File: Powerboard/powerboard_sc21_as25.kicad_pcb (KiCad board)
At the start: 4 copper layers, 86.1 x 55.6 mm, 172 parts, among them IC1 BQ24618RGET-iclr, IC2 CP2102, J1 Thermistor Connection 103AT N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, J10 Conn_01x04_Male, J2 Conn_01x02_Male, J3 Conn_01x02_Male, J4 Conn_01x08_Male, J5 Conn_01x04_Male, J6 Conn_01x02_Male, J7 IsolationSwitch, J8 USB_C_Receptacle_USB2.0, J9 Conn_Coaxial, Q1 RSJ250P10TL, Q10 MCH6351, Q2 RSJ250P10TL, Q3 RSJ250P10TL, Q4 RS1G120MN, Q5 RS1G120MN, Q6 MMDT2222A, Q7 RSJ250P10TL, Q8 RSJ250P10TL, Q9 MCH6351, U1 LTC4412xS6, U11 LTC4411, U2 SN65HVD230, U3 ESP32-PICO-D4, U4 RT9025-25GSP, U6 LM2679T-3.3-iclr, U7 LM2679T-3.3-iclr, U8 LTC4412xS6, U9 LTC4412xS6

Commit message: layout progress
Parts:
- C31, C32, R30, R31, U4: moved to B.Cu
- D7, R36, R37, TP23, TP24: moved to F.Cu
- RAC1: value 10mΩ -> FCSL110R010FER; footprint Resistor_SMD:R_0603_1608Metric -> iclr:RESC50110X50N
- moved U8 76.2 mm to (129.8, 72.7)
- moved C48 75.4 mm to (127.0, 72.9), turned to -90 degrees
- moved Q10 72.7 mm to (127.5, 75.8), turned to 180 degrees
- moved C44 69.2 mm to (131.3, 64.4), turned to -90 degrees
- moved D5 66.5 mm to (128.3, 66.8)
- moved C9 63.9 mm to (72.1, 69.4), turned to 0 degrees
- moved C8 62.5 mm to (72.2, 67.4), turned to 0 degrees
- moved C37 61.4 mm to (116.0, 61.9), turned to 180 degrees
- moved U7 60.9 mm to (118.2, 52.5), turned to 90 degrees
- moved C49 60.0 mm to (126.1, 49.9)
- moved U9 59.9 mm to (126.6, 52.3)
- moved Q9 59.8 mm to (130.1, 52.4), turned to -90 degrees
- moved C42 59.3 mm to (104.9, 45.8), turned to 0 degrees
- moved C45 57.9 mm to (122.8, 42.7), turned to -90 degrees
- moved TP19 57.1 mm to (10.1, 43.3)
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- renumbered C15 to Crr
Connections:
- C3 pad 1: Net-(C3-Pad1) -> Net-(C33-Pad2)
- C33 pad 2: Net-(C3-Pad1) -> Net-(C33-Pad2)
- IC1 pad 2: Net-(C3-Pad1) -> Net-(C33-Pad2)
- J4 pad 1: /CANH -> GND
- J4 pad 2: /CANH -> GND
- J4 pad 4: Net-(J4-Pad4) -> /CANL
- J4 pad 5: +3V3 -> Net-(J4-Pad5)
- J4 pad 6: +3V3 -> Net-(J4-Pad5)
- J4 pad 7: /CANL -> +3V3
- J4 pad 8: /CANL -> /CANH
- Q2 pad 3: Net-(C3-Pad1) -> Net-(C33-Pad2)
- Q7 pad 3: Net-(J4-Pad4) -> Net-(Q7-Pad3)
- RAC1 pad 1: +24V -> Net-(C33-Pad2)
- RAC1 pad 2: Net-(C3-Pad1) -> +24V
- U1 pad 6: Net-(J4-Pad4) -> Net-(Q7-Pad3)
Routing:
- net +24V: track 0.00 -> 150.5 mm, vias 0 -> 2
- net /SDA: track 0.00 -> 74.0 mm, vias 0 -> 2
- net +3V3: track 10.7 -> 84.3 mm
- net /Battery Charger/Q3-S: track 0.00 -> 64.6 mm, vias 0 -> 2
- net /SCL: track 0.00 -> 64.2 mm, vias 0 -> 2
- net /BATTSTAT2: track 0.00 -> 60.2 mm, vias 0 -> 1
- net /CHARGE: track 0.13 -> 58.4 mm
- net /BATTSTAT1: track 0.00 -> 55.7 mm, vias 0 -> 1
- net /3.3STAT2: track 0.00 -> 54.1 mm, vias 0 -> 3
- net Net-(IC1-Pad23): track 0.00 -> 54.0 mm, vias 0 -> 2
- net /Battery Charger/Q1-D: track 0.00 -> 52.7 mm
- net Net-(C39-Pad1): track 0.00 -> 49.7 mm
- net /BOOT: track 0.00 -> 48.9 mm, vias 0 -> 4
- net /3.3STAT1: track 0.00 -> 44.0 mm, vias 0 -> 3
- net Net-(C18-Pad2): track 0.00 -> 42.8 mm, vias 0 -> 2
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- added copper zone on F.Cu, net Net-(C31-Pad1)
- added copper zone on F.Cu, net Net-(J5-Pad1)
- added copper zone on F.Cu, net Net-(Q7-Pad3)

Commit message: update
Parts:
- removed Crr: 0.1µF, Capacitor_SMD:C_0603_1608Metric
- removed TP1, TP10, TP11, TP12, TP13, TP16, TP17, TP18, TP19, TP2, TP20, TP21, TP22, TP26, TP27, TP3, TP4, TP5, TP6, TP7, TP8, TP9: TestPoint, TestPoint:TestPoint_Pad_D1.0mm
- added C15: 0.1µF, Capacitor_SMD:C_0603_1608Metric, F.Cu at (72.6, 71.9)
- moved PackLED1 10.4 mm to (72.8, 81.7), turned to 0 degrees
- moved C48 9.31 mm to (127.6, 63.6), turned to 0 degrees
- moved R28 8.97 mm to (69.8, 81.7), turned to 180 degrees
- moved U8 6.83 mm to (128.2, 66.0)
- moved Q10 6.67 mm to (127.7, 69.2)
- moved D5 6.23 mm to (130.0, 72.8), turned to -90 degrees
- moved C17 2.17 mm to (96.3, 46.1)
- moved R6 2.17 mm to (94.8, 46.1)
- moved C1 1.90 mm to (80.2, 31.7), turned to 90 degrees
- moved C49 1.87 mm to (127.2, 48.4)
- moved C2 1.63 mm to (96.3, 43.1)
- moved R4 1.63 mm to (94.8, 43.1)
- moved C53 1.58 mm to (63.3, 68.1)
- moved C21 0.93 mm to (93.3, 66.3)
- moved C24 0.79 mm to (87.3, 47.1)
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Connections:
- J8 pad A1: Net-(J8-PadA1) -> GND
- J8 pad A12: Net-(J8-PadA1) -> GND
- J8 pad B1: Net-(J8-PadA1) -> GND
- J8 pad B12: Net-(J8-PadA1) -> GND
- J8 pad S1: unconnected-(J8-PadS1) -> GND
- PowerLED1 pad 2: Net-(PowerLED1-Pad2) -> Net-(J5-Pad1)
- Q1 pad 3: Net-(PowerLED1-Pad2) -> Net-(J5-Pad1)
- R20 pad 2: Net-(PowerLED1-Pad2) -> Net-(J5-Pad1)
- U3 pad 16: unconnected-(U3-Pad16) -> GND
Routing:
- net /EN: track 0.00 -> 70.3 mm, vias 0 -> 6
- net GND: track 1.11 -> 71.1 mm, vias 0 -> 19
- net Net-(IC1-Pad3): track 0.00 -> 69.3 mm, vias 0 -> 2
- net /Battery Charger/VFB: track 2.96 -> 71.8 mm, vias 0 -> 2
- net Net-(C17-Pad2): track 0.00 -> 60.2 mm, vias 0 -> 2
- net VBUS: track 7.41 -> 49.2 mm
- net /Battery Charger/VCC: track 0.00 -> 34.9 mm, vias 0 -> 2
- net /Battery Charger/Q3-S: track 64.6 -> 99.1 mm, vias 2 -> 8
- net Net-(Q7-Pad1): track 0.00 -> 30.4 mm, vias 0 -> 2
- net +3V3: track 84.3 -> 105.5 mm, vias 0 -> 19
- net Net-(IC1-Pad11): track 0.00 -> 18.9 mm
- net /Battery Charger/ACSET: track 0.00 -> 18.6 mm
- net Net-(C39-Pad1): track 49.7 -> 67.3 mm
- net /Battery Charger/ICSET2: track 0.00 -> 16.6 mm
- net Net-(Q7-Pad3): track 0.00 -> 15.9 mm
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- added copper zone on F.Cu, net +24V
- added copper zone on In2.Cu, net +3V3
- added copper zone on F.Cu, net /Battery Charger/Q3-S
- added copper zone on B.Cu, net GND
- added copper zone on F.Cu, net GND
- added copper zone on In1.Cu, net GND
- added copper zone on F.Cu, net Net-(C3-Pad1)

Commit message: update
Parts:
- C1, C10, C11, C3, C31, C33: value 0.1μF -> 0.1uF
- C14, C15, C48, C49, C6: value 0.1µF -> 0.1uF
- C17, C18, C2, C4: value 1μF -> 1uF
- C32: value 22μF -> 22uF; footprint Capacitor_SMD:C_1210_3225Metric -> Capacitor_SMD:C_1206_3216Metric
- C43: value 0.47μF -> 0.47uF
- C50: value 1.0muF -> 1.0uF
- C51, C53: value 0.1muF -> 0.1uF
- C52: value 4.7muF -> 4.7uF
- C54, C57: footprint Capacitor_SMD:C_0805_2012Metric -> Capacitor_SMD:C_0603_1608Metric
- L1: value 6.8µH -> 6.8uH
- R1, R11, R4: value 10kΩ -> 10k
- R10: value 430kΩ -> 430k
- R14, R15, R3, R5, R7: value 100kΩ -> 100k
- R16: value 100Ω -> 100
- R17: value 10Ω -> 10
- R18, R32: value 1kΩ -> 1k
- R19, R21, R37, R6, R8: value 470Ω -> 470
- R2: value 110kΩ -> 110k
- R20: value 2Ω -> 2
- R28, R29: value 3.5k -> 3k
- R9: value 9.31kΩ -> 9.31k
- RAdp1: value 150kΩ -> 150k
- RFast1: value 32kΩ -> 32k
- RPre1: value 13kΩ -> 13k
- RSR1: value 10mΩ -> 10m
- U4: value RT9025-25GSP -> SC4216H
- moved H1 2.53 mm to (52.1, 43.6)
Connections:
- net Net-(D8-Pad3) renamed /USB To UART/D-
- net Net-(D8-Pad4) renamed /USB To UART/D+
- IC2 pad 29: unconnected-(IC2-Pad29) -> GND
- J4 pad 5: Net-(J4-Pad5) -> Net-(U1-Pad6)
- J4 pad 6: Net-(J4-Pad5) -> Net-(U1-Pad6)
- Q7 pad 3: Net-(Q7-Pad3) -> Net-(U1-Pad6)
- R22 pad 2: Net-(C21-Pad2) -> Net-(R22-Pad2)
- U1 pad 3: /LPC_24V -> unconnected-(U1-Pad3)
- U1 pad 6: Net-(Q7-Pad3) -> Net-(U1-Pad6)
- U2 pad 1: Net-(C21-Pad2) -> Net-(R22-Pad2)
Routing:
- net /LPC_24V: track 43.1 -> 0.00 mm, vias 3 -> 0
- net unconnected-(U1-Pad3): track 0.00 -> 42.7 mm, vias 0 -> 3
- net Net-(Q7-Pad3): track 15.9 -> 0.00 mm
- net Net-(U1-Pad6): track 0.00 -> 15.7 mm
- net /Battery Charger/Q3-S: track 99.1 -> 105.6 mm
- net GND: track 71.1 -> 65.5 mm, vias 19 -> 17
- net +3V3: track 105.5 -> 110.6 mm, vias 19 -> 20
- net Net-(R22-Pad2): track 0.00 -> 3.50 mm
- net Net-(C21-Pad2): track 3.50 -> 0.00 mm
- net /EN: track 70.3 -> 72.5 mm
- net /BOOT: track 61.4 -> 63.6 mm
- net +24V: track 153.7 -> 155.1 mm
- net Net-(J5-Pad1): track 8.94 -> 10.2 mm
- net /PG: track 45.9 -> 44.9 mm
- net /Battery Charger/SRP: track 22.3 -> 21.3 mm
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- added copper zone on F.Cu, net Net-(U1-Pad6)
- removed copper zone on F.Cu, net Net-(Q7-Pad3)

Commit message: update 2
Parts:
- removed C21: 160pF, Capacitor_SMD:C_0603_1608Metric
- moved C58 1.60 mm to (61.8, 40.6), turned to 0 degrees
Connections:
- U1 pad 3: unconnected-(U1-Pad3) -> /LPC_24V
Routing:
- net /LPC_24V: track 0.00 -> 43.0 mm, vias 0 -> 3
- net unconnected-(U1-Pad3): track 42.7 -> 0.00 mm, vias 3 -> 0
- net Net-(IC1-Pad3): track 68.6 -> 63.3 mm
- net /Battery Charger/Q3-S: track 105.6 -> 102.9 mm, vias 8 -> 7
- net GND: track 65.5 -> 63.8 mm, vias 17 -> 18
- net Net-(R22-Pad2): track 3.50 -> 2.18 mm
- net /SCL: track 62.3 -> 63.2 mm
- net /CHARGE: track 59.7 -> 60.5 mm
- net /BATTSTAT1: track 57.9 -> 57.3 mm
- net /CANH: track 25.2 -> 24.6 mm
- net /CANL: track 39.5 -> 38.9 mm
- net Net-(IC1-Pad23): track 53.4 -> 52.9 mm

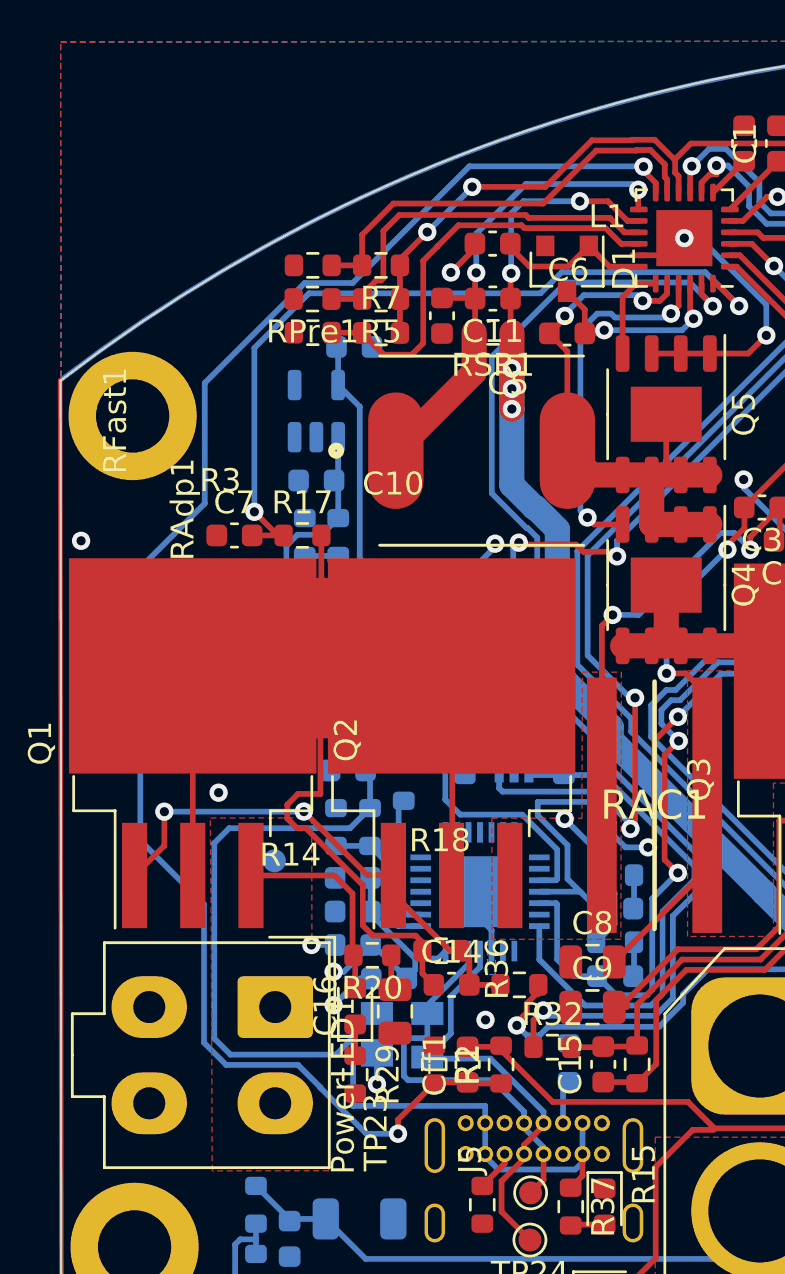
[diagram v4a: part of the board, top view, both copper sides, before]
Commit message: changed RSR traces to same layer
going to check charger layout recommendations again
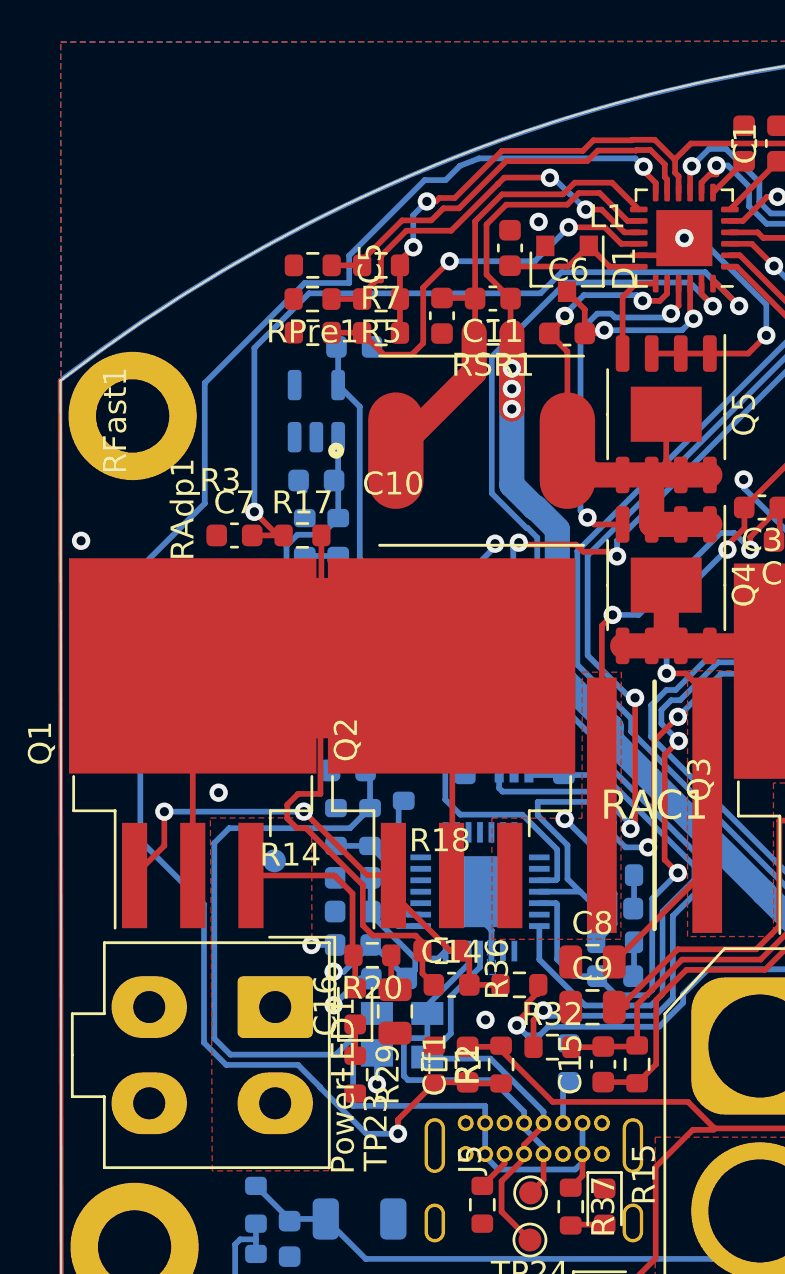
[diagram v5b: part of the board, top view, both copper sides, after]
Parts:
- moved C5 0.78 mm to (68.5, 36.2), turned to 90 degrees
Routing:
- net GND: track 63.8 -> 62.1 mm
- net /Battery Charger/Q3-S: track 102.9 -> 104.5 mm, vias 7 -> 5
- net /Battery Charger/VFB: track 71.5 -> 72.4 mm
- net /Battery Charger/CE: track 37.5 -> 38.2 mm
- net /Battery Charger/ICSET2: track 16.6 -> 17.4 mm, vias 0 -> 2
- net /Battery Charger/ACSET: track 18.6 -> 17.8 mm, vias 0 -> 2
- net Net-(IC1-Pad11): track 18.9 -> 18.3 mm
- net /Battery Charger/SRP: track 21.3 -> 21.2 mm, vias 2 -> 0

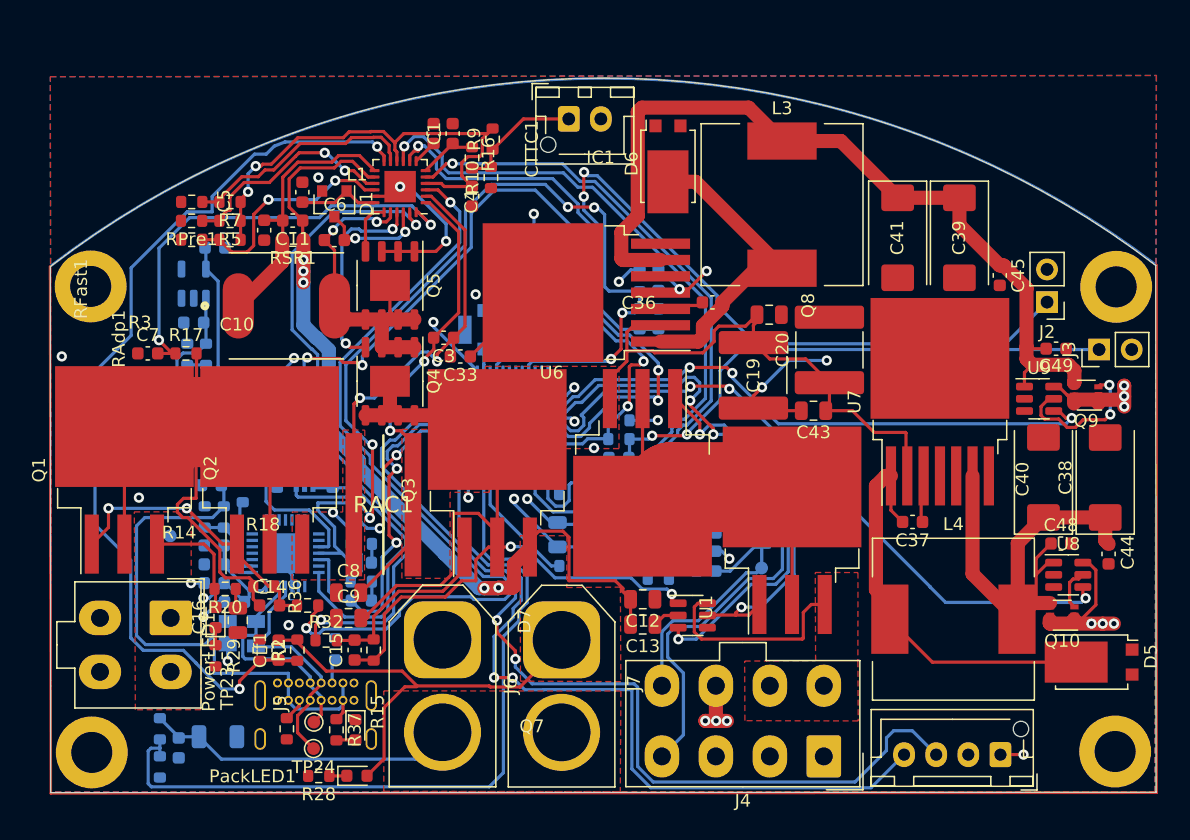
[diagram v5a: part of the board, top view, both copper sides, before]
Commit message: Andrei's review, no via fencing on ufl conn
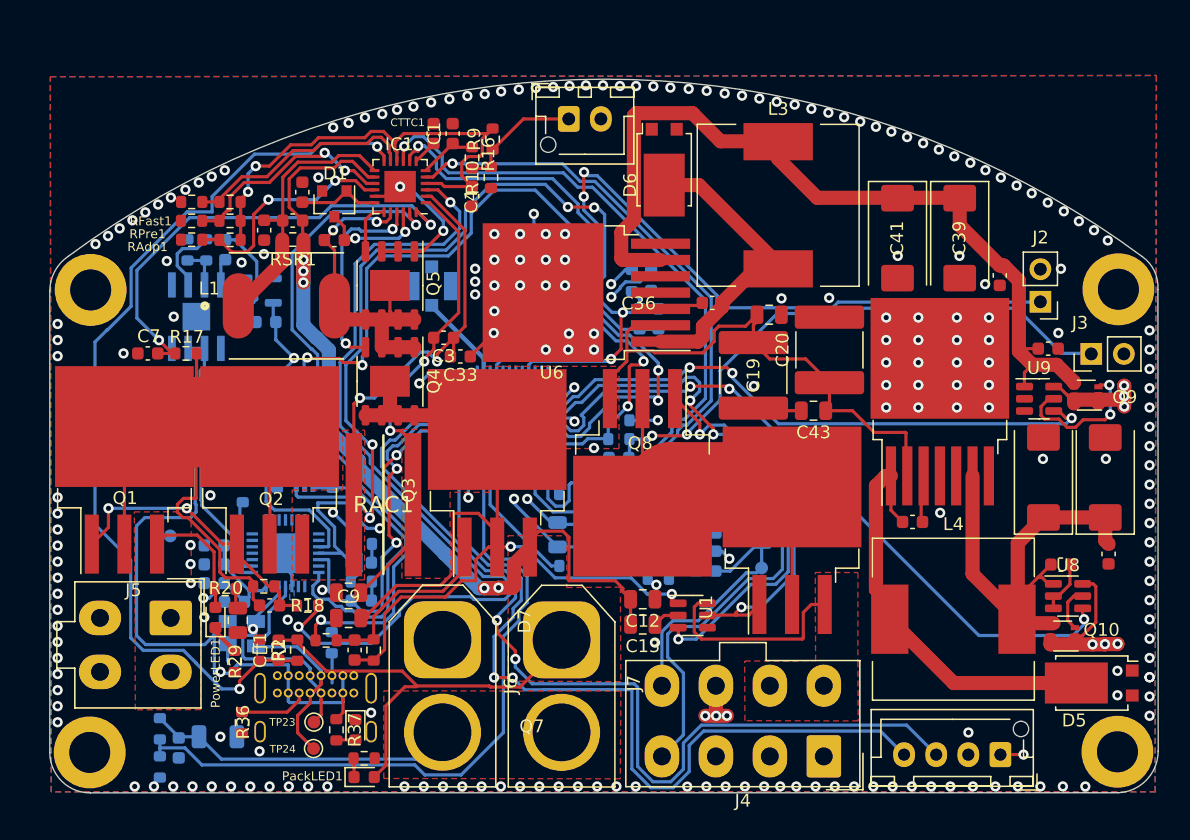
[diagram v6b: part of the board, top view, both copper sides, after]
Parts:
- moved R39 9.02 mm to (59.4, 52.6)
- moved R38 9.02 mm to (60.9, 52.6)
- moved C54 8.76 mm to (60.1, 50.4)
- moved U4 8.41 mm to (60.3, 45.9)
- moved R42 8.13 mm to (61.1, 40.7)
- moved R43 8.13 mm to (59.6, 40.7)
- moved C58 7.01 mm to (65.7, 46.4), turned to 180 degrees
- moved C57 6.18 mm to (62.5, 40.7), turned to 90 degrees
- moved J9 5.29 mm to (78.6, 43.5)
- moved U11 5.08 mm to (65.2, 43.9), turned to 0 degrees
- moved R28 3.79 mm to (73.4, 80.3), turned to 0 degrees
- moved R36 3.51 mm to (63.9, 77.5)
- moved U8 1.66 mm to (128.2, 67.7)
- moved C48 1.64 mm to (127.6, 65.2)
- moved D5 1.63 mm to (130.0, 74.5)
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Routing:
- net VBUS: track 49.2 -> 59.3 mm
- net Net-(IC2-Pad8): track 6.48 -> 16.2 mm
- net +3V3: track 110.8 -> 101.1 mm
- net GND: track 62.1 -> 55.0 mm, vias 18 -> 226
- net /CHARGE: track 60.5 -> 54.6 mm
- net /LNA_IN: track 1.68 -> 6.85 mm
- net Net-(C57-Pad2): track 9.34 -> 14.2 mm
- net Net-(IC1-Pad3): track 63.3 -> 67.9 mm
- net /EN: track 72.5 -> 76.5 mm
- net Net-(J8-PadB5): track 1.79 -> 5.39 mm
- net /BOOT: track 63.6 -> 66.7 mm
- net Net-(C18-Pad2): track 42.3 -> 45.1 mm
- net /SCL: track 63.2 -> 65.9 mm
- net Net-(C17-Pad2): track 60.2 -> 57.8 mm
- net /3.3STAT2: track 51.6 -> 53.1 mm
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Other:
- board size 86.1 x 55.6 mm -> 86.3 x 55.6 mm
- board text added: "Designed by Kiran de Silva Shiven Chandarana Andrei Paduraru Artem Sheykin"

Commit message: corrected based on bq24618 guidelines as much as possible
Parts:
- moved C3 6.81 mm to (79.4, 40.8)
- moved R35 0.85 mm to (70.0, 71.3)
- moved C33 0.66 mm to (80.2, 49.0)
- moved J1 0.59 mm to (88.7, 30.6)
- moved Q5 0.15 mm to (75.2, 43.6)
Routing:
- net GND: track 55.0 -> 46.1 mm, vias 226 -> 263
- net Net-(C3-Pad1): track 33.2 -> 31.5 mm
- net /Battery Charger/VFB: track 72.4 -> 71.2 mm
- net /Battery Charger/Q4-G: track 15.8 -> 16.7 mm
- net +24V: track 154.7 -> 155.6 mm
- net /Battery Charger/Q3-S: track 104.3 -> 103.7 mm, vias 5 -> 7
- net /USB To UART/D+: track 19.4 -> 18.8 mm
- net Net-(J1-Pad1): track 9.84 -> 9.30 mm
- net +3V3: track 101.1 -> 101.6 mm
- net (no net): vias 1 -> 0
